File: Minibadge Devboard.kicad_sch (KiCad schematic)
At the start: 41 parts, among them J1 External power, J2 External switch, Q1 PMOS, SW1 Power, SW3 SPEED, SW4 NTC, U1 DRV8837C, U2 74HC4060

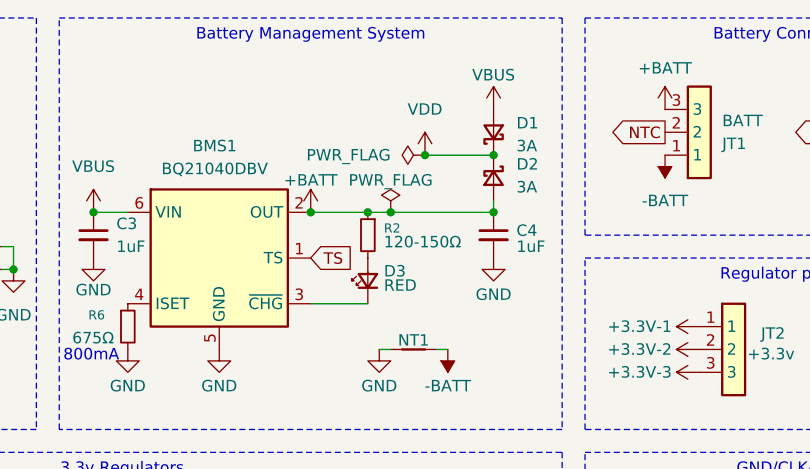
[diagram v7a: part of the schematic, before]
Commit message: Thermal vias for VREG
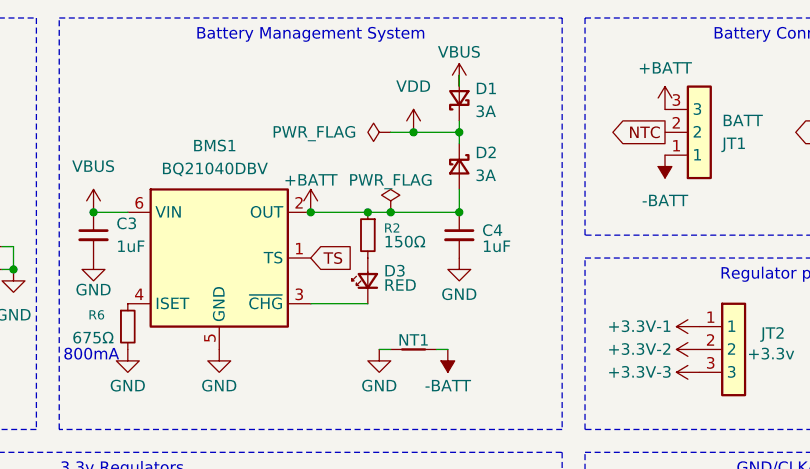
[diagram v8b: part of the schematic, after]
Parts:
- R2: value 120-150Ω -> 150Ω
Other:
- moved on the sheet: C4, D1, D2
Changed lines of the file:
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@@
 	)
 	(junction
-		(at 148.59 38.1)
+		(at 144.78 35.56)
 		(diameter 0)
 		(color 0 0 0 0)
@@
 	)
 	(junction
-		(at 87.63 35.56)
+		(at 139.7 35.56)
 		(diameter 0)
 		(color 0 0 0 0)
 	)
 	(junction
-		(at 104.14 44.45)
+		(at 87.63 35.56)
 		(diameter 0)
 		(color 0 0 0 0)
 	)
 	(junction
-		(at 99.06 82.55)
+		(at 104.14 44.45)
 		(diameter 0)
 		(color 0 0 0 0)
 	)
 	(junction
-		(at 140.97 38.1)
+		(at 99.06 82.55)
 		(diameter 0)
 		(color 0 0 0 0)
 	)
 	(junction
-		(at 148.59 44.45)
+		(at 144.78 44.45)
 		(diameter 0)
 		(color 0 0 0 0)
@@
 	(wire
 		(pts
-			(xy 140.97 38.1) (xy 148.59 38.1)
+			(xy 137.16 35.56) (xy 139.7 35.56)
+		)
+		(stroke
+			(width 0)
+			(type default)
+		)
+	)
+	(wire
+		(pts
+			(xy 144.78 36.83) (xy 144.78 35.56)
 		)
 		(stroke
@@
 	(wire
 		(pts
-			(xy 148.59 43.18) (xy 148.59 44.45)
+			(xy 144.78 41.91) (xy 144.78 44.45)
 		)
 		(stroke
@@
 	(wire
 		(pts
+			(xy 144.78 34.29) (xy 144.78 35.56)
+		)
+		(stroke
+			(width 0)
+			(type default)
+		)
+	)
+	(wire
+		(pts
+			(xy 139.7 35.56) (xy 144.78 35.56)
+		)
+		(stroke
+			(width 0)
+			(type default)
+		)
+	)
+	(wire
+		(pts
+			(xy 144.78 30.48) (xy 144.78 29.21)
+		)
+		(stroke
+			(width 0)
+			(type default)
+		)
+	)
+	(wire
+		(pts
 			(xy 76.2 114.3) (xy 76.2 111.76)
 		)
@@
 	(wire
 		(pts
-			(xy 137.16 44.45) (xy 148.59 44.45)
+			(xy 137.16 44.45) (xy 144.78 44.45)
 		)
 		(stroke
@@
 			)
 		)
-		(property "Value" "120-150Ω"
+		(property "Value" "150Ω"
 			(at 136.398 47.752 0)
 			(effects
@@
 	(symbol
 		(lib_id "power:VDD")
-		(at 140.97 38.1 0)
+		(at 139.7 35.56 0)
 		(unit 1)
 		(exclude_from_sim no)
@@
 		(fields_autoplaced yes)
 		(property "Reference" "#PWR045"
-			(at 140.97 41.91 0)
+			(at 139.7 39.37 0)
 			(effects
 				(font
@@
 		)
 		(property "Value" "VDD"
-			(at 140.97 33.02 0)
+			(at 139.7 30.48 0)
 			(effects
 				(font
@@
 		)
 		(property "Footprint" ""
-			(at 140.97 38.1 0)
+			(at 139.7 35.56 0)
 			(effects
 				(font
@@
 		)
 		(property "Datasheet" ""
-			(at 140.97 38.1 0)
+			(at 139.7 35.56 0)
 			(effects
 				(font
@@
 		)
 		(property "Description" "Power symbol creates a global label with name \"VDD\""
-			(at 140.97 38.1 0)
+			(at 139.7 35.56 0)
 			(effects
 				(font
@@
 	(symbol
 		(lib_id "Device:D_Schottky_Small")
-		(at 148.59 40.64 270)
+		(at 144.78 39.37 270)
 		(unit 1)
 		(exclude_from_sim no)
@@
 		(on_board yes)
 		(dnp no)
-		(fields_autoplaced yes)
 		(property "Reference" "D2"
-			(at 151.13 39.1159 90)
+			(at 146.558 37.846 90)
 			(effects
 				(font
@@
 		)
 		(property "Value" "3A"
-			(at 151.13 41.6559 90)
+			(at 146.558 40.386 90)
 			(effects
 				(font
@@
 		)
 		(property "Footprint" "Diode_SMD:D_SMA"
-			(at 148.59 40.64 90)
+			(at 144.78 39.37 90)
 			(effects
 				(font
@@
 		)
 		(property "Datasheet" "~"
-			(at 148.59 40.64 90)
+			(at 144.78 39.37 90)
 			(effects
 				(font
@@
 		)
 		(property "Description" "Schottky diode, small symbol"
-			(at 148.59 40.64 0)
+			(at 144.78 39.37 0)
 			(effects
 				(font
@@
 		)
 		(property "LCSC Part #" "C382787"
-			(at 148.59 40.64 90)
+			(at 144.78 39.37 90)
 			(effects
 				(font
@@
 	(symbol
 		(lib_id "power:VBUS")
-		(at 148.59 33.02 0)
+		(at 144.78 30.48 0)
 		(unit 1)
 		(exclude_from_sim no)
@@
 		(dnp no)
 		(property "Reference" "#PWR04"
-			(at 148.59 36.83 0)
+			(at 144.78 34.29 0)
 			(effects
 				(font
@@
 		)
 		(property "Value" "VBUS"
-			(at 148.59 29.21 0)
+			(at 144.78 26.67 0)
 			(effects
 				(font
@@
 		)
 		(property "Footprint" ""
-			(at 148.59 33.02 0)
+			(at 144.78 30.48 0)
 			(effects
 				(font
@@
 		)
 		(property "Datasheet" ""
-			(at 148.59 33.02 0)
+			(at 144.78 30.48 0)
 			(effects
 				(font
@@
 		)
 		(property "Description" "Power symbol creates a global label with name \"VBUS\""
-			(at 148.59 33.02 0)
+			(at 144.78 30.48 0)
 			(effects
 				(font
@@
 	(symbol
 		(lib_id "power:GND")
-		(at 148.59 49.53 0)
+		(at 144.78 49.53 0)
 		(unit 1)
 		(exclude_from_sim no)
@@
 		(dnp no)
 		(property "Reference" "#PWR016"
-			(at 148.59 55.88 0)
+			(at 144.78 55.88 0)
 			(effects
 				(font
@@
 		)
 		(property "Value" "GND"
-			(at 148.59 53.594 0)
+			(at 144.78 53.594 0)
 			(effects
 				(font
@@
 		)
 		(property "Footprint" ""
-			(at 148.59 49.53 0)
+			(at 144.78 49.53 0)
 			(effects
 				(font
@@
 		)
 		(property "Datasheet" ""
-			(at 148.59 49.53 0)
+			(at 144.78 49.53 0)
 			(effects
 				(font
@@
 		)
 		(property "Description" "Power symbol creates a global label with name \"GND\" , ground"
-			(at 148.59 49.53 0)
+			(at 144.78 49.53 0)
 			(effects
 				(font
@@
 	(symbol
 		(lib_id "Device:C_Small")
-		(at 148.59 46.99 0)
+		(at 144.78 46.99 0)
 		(unit 1)
 		(exclude_from_sim no)
@@
 		(dnp no)
 		(property "Reference" "C4"
-			(at 151.13 46.482 0)
+			(at 147.32 46.482 0)
 			(effects
 				(font
@@
 		)
 		(property "Value" "1uF"
-			(at 151.13 48.2662 0)
+			(at 147.32 48.2662 0)
 			(effects
 				(font
@@
 		)
 		(property "Footprint" "Capacitor_SMD:C_0603_1608Metric"
-			(at 148.59 46.99 0)
+			(at 144.78 46.99 0)
 			(effects
 				(font
@@
 		)
 		(property "Datasheet" "~"
-			(at 148.59 46.99 0)
+			(at 144.78 46.99 0)
 			(effects
 				(font
@@
 		)
 		(property "Description" "Unpolarized capacitor, small symbol"
-			(at 148.59 46.99 0)
+			(at 144.78 46.99 0)
 			(effects
 				(font
@@
 		)
 		(property "Sim.Type" ""
-			(at 148.59 46.99 0)
+			(at 144.78 46.99 0)
 			(effects
 				(font
@@
 		)
 		(property "LCSC Part #" "C15849"
-			(at 148.59 46.99 0)
+			(at 144.78 46.99 0)
 			(effects
 				(font
@@
 	(symbol
 		(lib_id "Device:D_Schottky_Small")
-		(at 148.59 35.56 90)
+		(at 144.78 31.75 90)
 		(unit 1)
 		(exclude_from_sim no)
@@
 		(on_board yes)
 		(dnp no)
-		(fields_autoplaced yes)
 		(property "Reference" "D1"
-			(at 151.13 34.5439 90)
+			(at 146.558 30.734 90)
 			(effects
 				(font
@@
 		)
 		(property "Value" "3A"
-			(at 151.13 37.0839 90)
+			(at 146.558 33.274 90)
 			(effects
 				(font
@@
 		)
 		(property "Footprint" "Diode_SMD:D_SMA"
-			(at 148.59 35.56 90)
+			(at 144.78 31.75 90)
 			(effects
 				(font
@@
 		)
 		(property "Datasheet" "~"
-			(at 148.59 35.56 90)
+			(at 144.78 31.75 90)
 			(effects
 				(font
@@
 		)
 		(property "Description" "Schottky diode, small symbol"
-			(at 148.59 35.56 0)
+			(at 144.78 31.75 0)
 			(effects
 				(font
@@
 		)
 		(property "LCSC Part #" "C382787"
-			(at 148.59 35.56 90)
+			(at 144.78 31.75 90)
 			(effects
 				(font
@@
 	(symbol
 		(lib_id "power:PWR_FLAG")
-		(at 140.97 38.1 90)
+		(at 137.16 35.56 90)
 		(unit 1)
 		(exclude_from_sim no)
@@
 		(fields_autoplaced yes)
 		(property "Reference" "#FLG04"
-			(at 139.065 38.1 0)
+			(at 135.255 35.56 0)
 			(effects
 				(font
@@
 		)
 		(property "Value" "PWR_FLAG"
-			(at 137.16 38.0999 90)
+			(at 133.35 35.5599 90)
 			(effects
 				(font
@@
 		)
 		(property "Footprint" ""
-			(at 140.97 38.1 0)
+			(at 137.16 35.56 0)
 			(effects
 				(font
@@
 		)
 		(property "Datasheet" "~"
-			(at 140.97 38.1 0)
+			(at 137.16 35.56 0)
 			(effects
 				(font
@@
 		)
 		(property "Description" "Special symbol for telling ERC where power comes from"
-			(at 140.97 38.1 0)
+			(at 137.16 35.56 0)
 			(effects
 				(font
